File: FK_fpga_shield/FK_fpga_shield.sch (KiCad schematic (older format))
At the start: 168 parts, among them J0 USB_B_Mini, J1 molex-51382-0400-microclasp, J10 molex-51382-0400-microclasp, J11 molex-51382-0400-microclasp, J12 molex-51382-0400-microclasp, J13 molex-51382-0400-microclasp, J14 molex-51382-0400-microclasp, J15 molex-51382-0400-microclasp, J16 molex-51382-0400-microclasp, J17 molex-51382-0400-microclasp, J18 molex-51382-0400-microclasp, J19 molex-51382-0400-microclasp, J2 molex-51382-0400-microclasp, J20 molex-51382-0400-microclasp, J21 molex-51382-0400-microclasp, J22 molex-51382-0400-microclasp, J23 molex-51382-0400-microclasp, J24 molex-51382-0400-microclasp, J25 molex-51382-0400-microclasp, J26 molex-51382-0400-microclasp, J27 molex-51382-0400-microclasp, J28 molex-51382-0400-microclasp, J29 molex-51382-0400-microclasp, J3 molex-51382-0400-microclasp, J30 molex-51382-0400-microclasp, J31 molex-51382-0400-microclasp, J32 molex-51382-0400-microclasp, J33 molex-51382-0400-microclasp, J34 molex-51382-0400-microclasp, J35 molex-51382-0400-microclasp, J36 Barrel_Jack_MountingPin, J37 Conn_02x04_Top_Bottom, J4 molex-51382-0400-microclasp, J5 molex-51382-0400-microclasp, J6 molex-51382-0400-microclasp, J7 molex-51382-0400-microclasp, J8 molex-51382-0400-microclasp, J9 molex-51382-0400-microclasp, U1 FT232RL, U2 nvt2010pw, U3 nvt2010pw, U4 nvt2010pw, U5 nvt2010pw, U6 nvt2010pw, U7 nvt2010pw, U8 nvt2010pw, Y1 DNP_(12MHz)

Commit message: various minor
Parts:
- removed L1: WE_744823422, Inductor_THT:L_CommonMode_Wuerth_WE-CMB-M, symbol Device:L_Core_Iron_Coupled_1243
- added FL1: BNX016-01, FK_fpga_shield_custom_footprints:FIL_BNX016-01, symbol FK_fpga_shield_custom_symbols:BNX016-01
- C4: footprint Capacitor_SMD:C_0805_2012Metric_Pad1.15x1.40mm_HandSolder -> Capacitor_THT:CP_Radial_D4.0mm_P1.50mm
- J1, J10, J11, J12, J13, J14, J15, J16, J17, J18, J19, J2, J20, J21, J22, J23, J24, J25, J26, J27, J28, J29, J3, J30, J31, J32, J33, J34, J35, J4, J5, J6, J7, J8, J9: footprint FK_fpga_shield_custom_footprints:Molex_MicroClasp_55935-0410_1x04_P2.00mm_Horizontal_3DMODEL -> Connector_Molex:Molex_MicroClasp_55935-0410_1x04_P2.00mm_Horizontal
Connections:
- net 5V: now also FL1.2
- net GND: now also FL1.4, FL1.5, FL1.6
- net at J36.1: now also FL1.1
- net at J36.2, J36.MP (MountPin): now also FL1.3
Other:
- note added: "TODO:\nsilkscreen"
- note removed: "TODO:\nresistor values\nmove choke?\nsilkscreen etc\nBNX016-01"
- moved on the sheet: J36

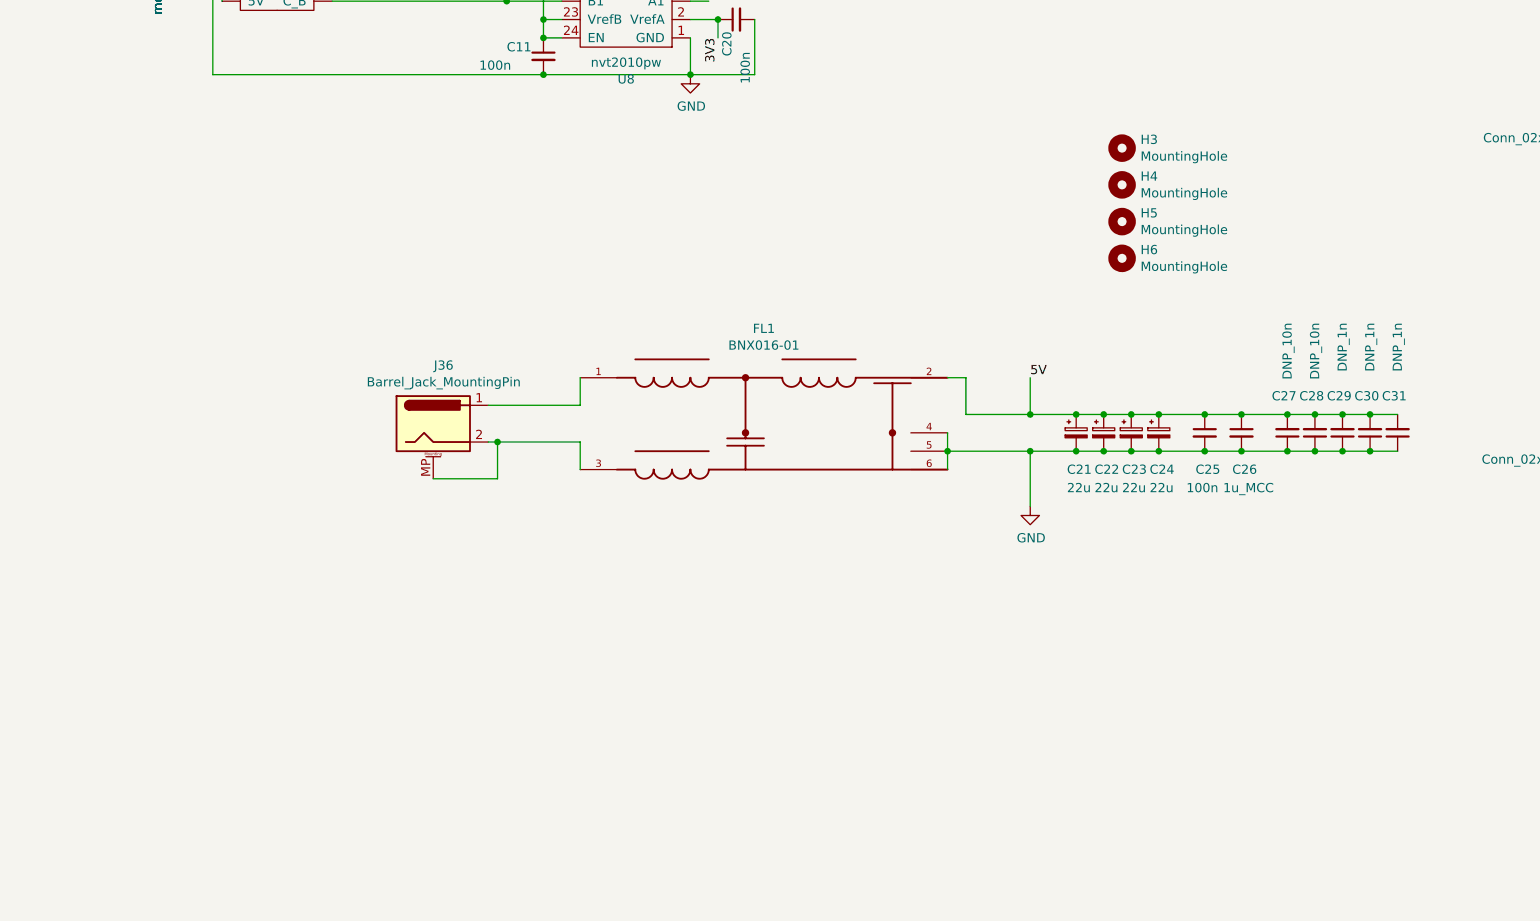
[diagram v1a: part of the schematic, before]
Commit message: mounting holes, silkscreen
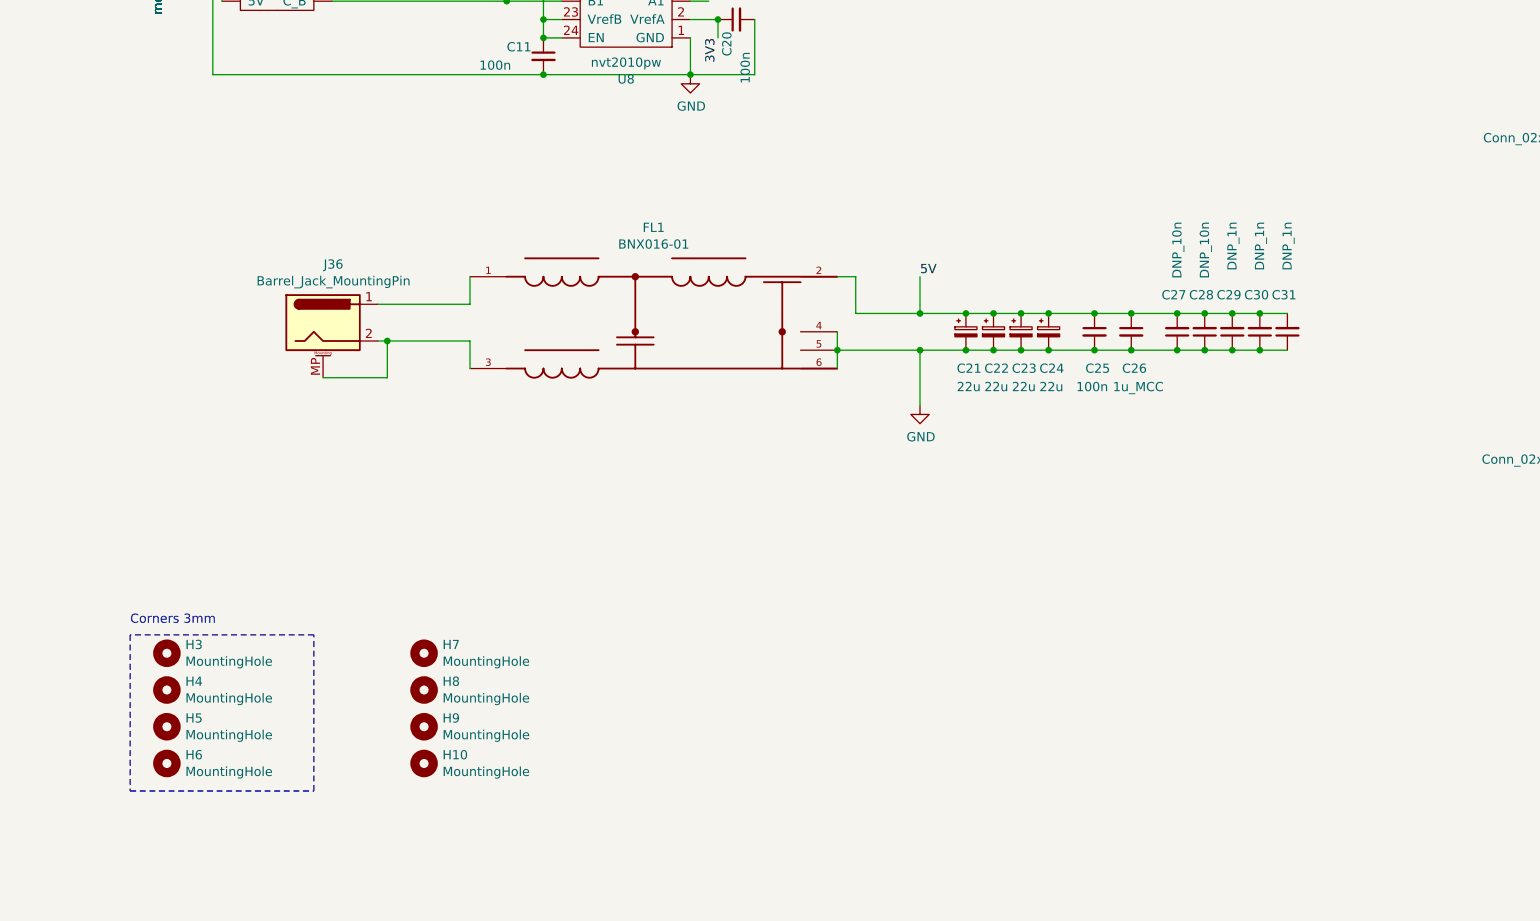
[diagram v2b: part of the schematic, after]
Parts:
- added H10, H7, H8, H9: MountingHole, MountingHole:MountingHole_3.2mm_M3, symbol Mechanical:MountingHole
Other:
- note added: "Corners 3mm"
- moved on the sheet: C21, C22, C23, C24, C25, C26, C27, C28, C29, C30, C31, FL1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

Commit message: gerbers etc
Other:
- note removed: "TODO:\nsilkscreen"
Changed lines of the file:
@@
 Text Label 14250 2950 0    50   ~ 0
 3V3
-Text Notes 16650 7750 0    1181 ~ 0
-TODO:\nsilkscreen
 $Comp
 L FK_fpga_shield_custom_symbols:BNX016-01 FL1

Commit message: turning off
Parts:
- J0: symbol Connector:USB_B_Mini -> FK_fpga_shield-rescue:USB_B_Mini-Connector
- R1: value 4k7 -> 51k
- R2: value 10k -> 100k
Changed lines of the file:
@@
 RX
 $Comp
-L Connector:USB_B_Mini J0
+L FK_fpga_shield-rescue:USB_B_Mini-Connector J0
 U 1 1 603AFCC4
 P 10050 1700
@@
 P 10700 2000
 F 0 "R1" H 10759 2046 50  0000 L CNN
-F 1 "4k7" H 10759 1955 50  0000 L CNN
+F 1 "51k" H 10759 1955 50  0000 L CNN
 F 2 "Resistor_SMD:R_0805_2012Metric_Pad1.15x1.40mm_HandSolder" H 10700 2000 50  0001 C CNN
 F 3 "~" H 10700 2000 50  0001 C CNN
@@
 P 10700 2200
 F 0 "R2" H 10759 2246 50  0000 L CNN
-F 1 "10k" H 10759 2155 50  0000 L CNN
+F 1 "100k" H 10759 2155 50  0000 L CNN
 F 2 "Resistor_SMD:R_0805_2012Metric_Pad1.15x1.40mm_HandSolder" H 10700 2200 50  0001 C CNN
 F 3 "~" H 10700 2200 50  0001 C CNN
